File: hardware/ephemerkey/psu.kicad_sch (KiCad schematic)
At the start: 24 parts, among them J3 USB-C, J4 BAT 1S Li-ion, J5 USB-C (vert), Q1 AO3401A, U2 TPS63900DSKR, U3 USBLC6-2SC6, U4 MCP73831-2-OT

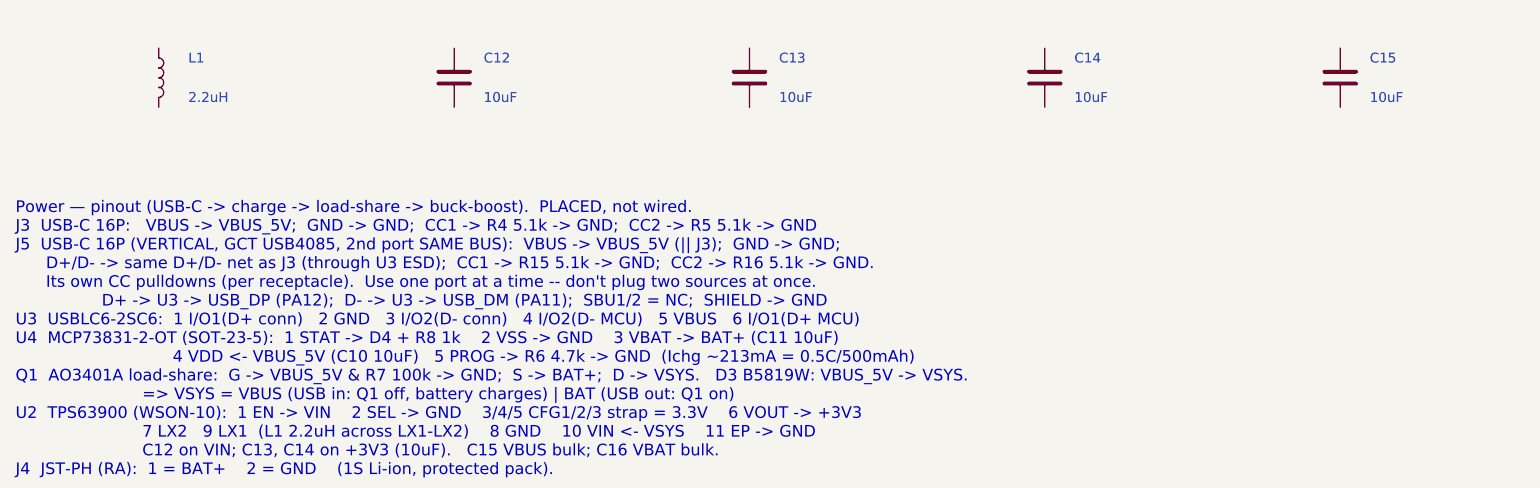
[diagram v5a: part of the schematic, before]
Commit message: ephemerkey: 2nd USB-C -> vertical GT-USB-7051A (C2843970), KiCad footprint
USB4085 was horizontal (GCT drawing: 'Dip Type, PCB Top Mount' -- cable inserts
parallel to the board), not the upright connector needed. Swap J5 to the
G-Switch GT-USB-7051A (C2843970): true vertical/upright SMT USB-C that sticks up
off the board, 16-pin USB2.0, ~3.5k JLCPCB stock, with a bundled KiCad footprint
(USB_C_Receptacle_G-Switch_GT-USB-7051x) + 3D model. Same symbol/bus as J3.

Co-Authored-By: Claude Opus 4.8 (1M context) <noreply@anthropic.com>
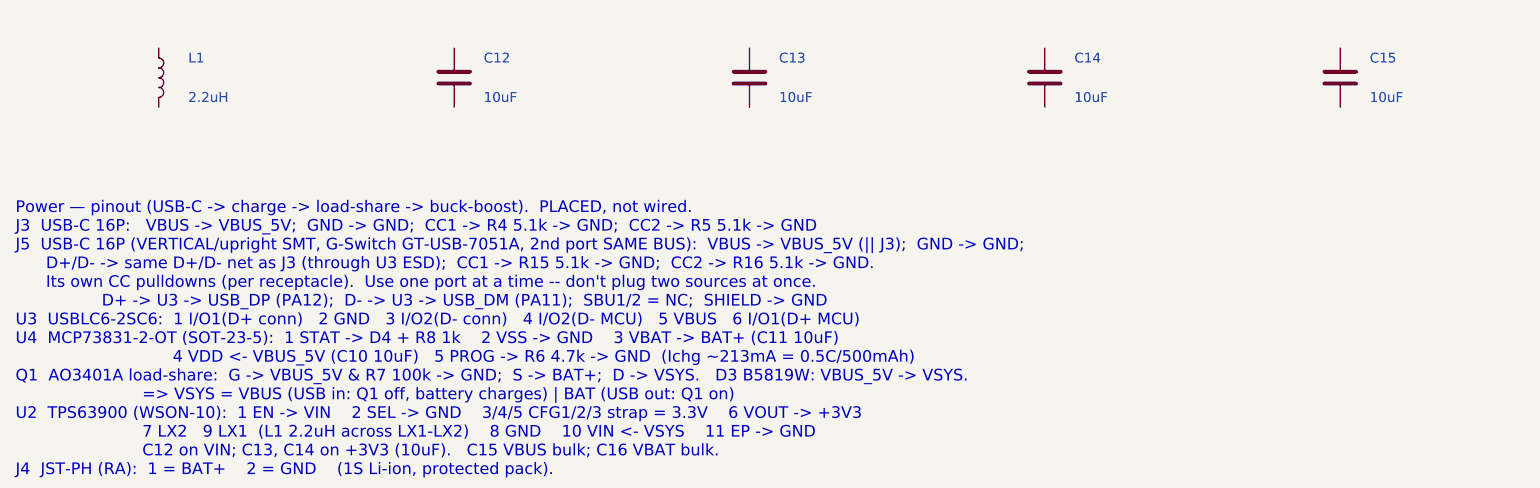
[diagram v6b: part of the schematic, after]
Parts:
- J5: footprint Connector_USB:USB_C_Receptacle_GCT_USB4085 -> Connector_USB:USB_C_Receptacle_G-Switch_GT-USB-7051x; LCSC C7095263 -> C2843970; MPN USB4085-GF-A -> GT-USB-7051A; Manufacturer GCT -> G-Switch
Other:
- note added: "Power — pinout (USB-C -> charge -> load-share -> buck-boost). PLACED, not wired. J3 USB-C 16P: VBUS -> VBUS_5V; GND -> GND; CC1 -> R4 5.1k -> GND; CC2 -> R5 5.1k -> GND J5 USB-C 16P (VERTICAL/upright SMT, G-Switch GT-USB-7051A, 2nd port SAME BUS): VBUS -> VBUS_5V (|| J3); GND -> GND; D+/D- -> same D+/D- net as J3 (through U3 ESD); CC1 -> R15 5.1k -> GND; CC2 -> R16 5.1k -> GND. Its own CC pulldow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"
- note removed: "Power — pinout (USB-C -> charge -> load-share -> buck-boost). PLACED, not wired. J3 USB-C 16P: VBUS -> VBUS_5V; GND -> GND; CC1 -> R4 5.1k -> GND; CC2 -> R5 5.1k -> GND J5 USB-C 16P (VERTICAL, GCT USB4085, 2nd port SAME BUS): VBUS -> VBUS_5V (|| J3); GND -> GND; D+/D- -> same D+/D- net as J3 (through U3 ESD); CC1 -> R15 5.1k -> GND; CC2 -> R16 5.1k -> GND. Its own CC pulldowns (per receptacle). U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"

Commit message: ephemerkey: vendor 3D model for the vertical USB-C (GT-USB-7051A)
The KiCad footprint for GT-USB-7051x references a STEP that's absent from this
(partial) 3D-model install. Fetched the model for C2843970 via easyeda2kicad
(EasyEDA/LCSC) -> lib/3dmodels/USB_C_GT-USB-7051A.step (2.3MB STEP), and added a
project footprint copy ephemerkey:USB_C_Receptacle_G-Switch_GT-USB-7051x with its
(model ...) repointed at the vendored file. J5 now uses the project footprint.
Verify model offset/rotation in the 3D viewer at layout (EasyEDA origin).

Co-Authored-By: Claude Opus 4.8 (1M context) <noreply@anthropic.com>
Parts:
- J5: footprint Connector_USB:USB_C_Receptacle_G-Switch_GT-USB-7051x -> ephemerkey:USB_C_Receptacle_G-Switch_GT-USB-7051x
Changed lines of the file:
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@@
 		(instances
 			(project "ephemerkey"
-				(path "/e1000000-0000-4000-8000-000000000001/9c958eea-92af-4fab-91f9-b500de8c2eb3"
+				(path "/e1000000-0000-4000-8000-000000000001/1a9d986c-45f1-4170-b653-57058bfaa0ea"
 					(reference "J3")
 					(unit 1)
@@
 		(instances
 			(project "ephemerkey"
-				(path "/e1000000-0000-4000-8000-000000000001/9c958eea-92af-4fab-91f9-b500de8c2eb3"
+				(path "/e1000000-0000-4000-8000-000000000001/1a9d986c-45f1-4170-b653-57058bfaa0ea"
 					(reference "J4")
 					(unit 1)
@@
 		(instances
 			(project "ephemerkey"
-				(path "/e1000000-0000-4000-8000-000000000001/9c958eea-92af-4fab-91f9-b500de8c2eb3"
+				(path "/e1000000-0000-4000-8000-000000000001/1a9d986c-45f1-4170-b653-57058bfaa0ea"
 					(reference "U2")
 					(unit 1)
@@
 			(effects (font (size 1.27 1.27)) (justify left))
 		)
-		(property "Footprint" "Connector_USB:USB_C_Receptacle_G-Switch_GT-USB-7051x"
+		(property "Footprint" "ephemerkey:USB_C_Receptacle_G-Switch_GT-USB-7051x"
 			(at 335.2800 55.8800 0)
 			(effects (font (size 1.27 1.27))) (hide yes)
@@
 		(instances
 			(project "ephemerkey"
-				(path "/e1000000-0000-4000-8000-000000000001/9c958eea-92af-4fab-91f9-b500de8c2eb3"
+				(path "/e1000000-0000-4000-8000-000000000001/1a9d986c-45f1-4170-b653-57058bfaa0ea"
 					(reference "J5")
 					(unit 1)
@@
 		(instances
 			(project "ephemerkey"
-				(path "/e1000000-0000-4000-8000-000000000001/9c958eea-92af-4fab-91f9-b500de8c2eb3"
+				(path "/e1000000-0000-4000-8000-000000000001/1a9d986c-45f1-4170-b653-57058bfaa0ea"
 					(reference "U3")
 					(unit 1)
@@
 		(instances
 			(project "ephemerkey"
-				(path "/e1000000-0000-4000-8000-000000000001/9c958eea-92af-4fab-91f9-b500de8c2eb3"
+				(path "/e1000000-0000-4000-8000-000000000001/1a9d986c-45f1-4170-b653-57058bfaa0ea"
 					(reference "R4")
 					(unit 1)
@@
 		(instances
 			(project "ephemerkey"
-				(path "/e1000000-0000-4000-8000-000000000001/9c958eea-92af-4fab-91f9-b500de8c2eb3"
+				(path "/e1000000-0000-4000-8000-000000000001/1a9d986c-45f1-4170-b653-57058bfaa0ea"
 					(reference "R5")
 					(unit 1)
@@
 		(instances
 			(project "ephemerkey"
-				(path "/e1000000-0000-4000-8000-000000000001/9c958eea-92af-4fab-91f9-b500de8c2eb3"
+				(path "/e1000000-0000-4000-8000-000000000001/1a9d986c-45f1-4170-b653-57058bfaa0ea"
 					(reference "U4")
 					(unit 1)
@@
 		(instances
 			(project "ephemerkey"
-				(path "/e1000000-0000-4000-8000-000000000001/9c958eea-92af-4fab-91f9-b500de8c2eb3"
+				(path "/e1000000-0000-4000-8000-000000000001/1a9d986c-45f1-4170-b653-57058bfaa0ea"
 					(reference "R6")
 					(unit 1)
@@
 		(instances
 			(project "ephemerkey"
-				(path "/e1000000-0000-4000-8000-000000000001/9c958eea-92af-4fab-91f9-b500de8c2eb3"
+				(path "/e1000000-0000-4000-8000-000000000001/1a9d986c-45f1-4170-b653-57058bfaa0ea"
 					(reference "C10")
 					(unit 1)
@@
 		(instances
 			(project "ephemerkey"
-				(path "/e1000000-0000-4000-8000-000000000001/9c958eea-92af-4fab-91f9-b500de8c2eb3"
+				(path "/e1000000-0000-4000-8000-000000000001/1a9d986c-45f1-4170-b653-57058bfaa0ea"
 					(reference "C11")
 					(unit 1)
@@
 		(instances
 			(project "ephemerkey"
-				(path "/e1000000-0000-4000-8000-000000000001/9c958eea-92af-4fab-91f9-b500de8c2eb3"
+				(path "/e1000000-0000-4000-8000-000000000001/1a9d986c-45f1-4170-b653-57058bfaa0ea"
 					(reference "Q1")
 					(unit 1)
@@
 		(instances
 			(project "ephemerkey"
-				(path "/e1000000-0000-4000-8000-000000000001/9c958eea-92af-4fab-91f9-b500de8c2eb3"
+				(path "/e1000000-0000-4000-8000-000000000001/1a9d986c-45f1-4170-b653-57058bfaa0ea"
 					(reference "D3")
 					(unit 1)
@@
 		(instances
 			(project "ephemerkey"
-				(path "/e1000000-0000-4000-8000-000000000001/9c958eea-92af-4fab-91f9-b500de8c2eb3"
+				(path "/e1000000-0000-4000-8000-000000000001/1a9d986c-45f1-4170-b653-57058bfaa0ea"
 					(reference "R7")
 					(unit 1)
@@
 		(instances
 			(project "ephemerkey"
-				(path "/e1000000-0000-4000-8000-000000000001/9c958eea-92af-4fab-91f9-b500de8c2eb3"
+				(path "/e1000000-0000-4000-8000-000000000001/1a9d986c-45f1-4170-b653-57058bfaa0ea"
 					(reference "L1")
 					(unit 1)
@@
 		(instances
 			(project "ephemerkey"
-				(path "/e1000000-0000-4000-8000-000000000001/9c958eea-92af-4fab-91f9-b500de8c2eb3"
+				(path "/e1000000-0000-4000-8000-000000000001/1a9d986c-45f1-4170-b653-57058bfaa0ea"
 					(reference "C12")
 					(unit 1)
@@
 		(instances
 			(project "ephemerkey"
-				(path "/e1000000-0000-4000-8000-000000000001/9c958eea-92af-4fab-91f9-b500de8c2eb3"
+				(path "/e1000000-0000-4000-8000-000000000001/1a9d986c-45f1-4170-b653-57058bfaa0ea"
 					(reference "C13")
 					(unit 1)
@@
 		(instances
 			(project "ephemerkey"
-				(path "/e1000000-0000-4000-8000-000000000001/9c958eea-92af-4fab-91f9-b500de8c2eb3"
+				(path "/e1000000-0000-4000-8000-000000000001/1a9d986c-45f1-4170-b653-57058bfaa0ea"
 					(reference "C14")
 					(unit 1)
@@
 		(instances
 			(project "ephemerkey"
-				(path "/e1000000-0000-4000-8000-000000000001/9c958eea-92af-4fab-91f9-b500de8c2eb3"
+				(path "/e1000000-0000-4000-8000-000000000001/1a9d986c-45f1-4170-b653-57058bfaa0ea"
 					(reference "C15")
 					(unit 1)
@@
 		(instances
 			(project "ephemerkey"
-				(path "/e1000000-0000-4000-8000-000000000001/9c958eea-92af-4fab-91f9-b500de8c2eb3"
+				(path "/e1000000-0000-4000-8000-000000000001/1a9d986c-45f1-4170-b653-57058bfaa0ea"
 					(reference "C16")
 					(unit 1)
@@
 		(instances
 			(project "ephemerkey"
-				(path "/e1000000-0000-4000-8000-000000000001/9c958eea-92af-4fab-91f9-b500de8c2eb3"
+				(path "/e1000000-0000-4000-8000-000000000001/1a9d986c-45f1-4170-b653-57058bfaa0ea"
 					(reference "D4")
 					(unit 1)
@@
 		(instances
 			(project "ephemerkey"
-				(path "/e1000000-0000-4000-8000-000000000001/9c958eea-92af-4fab-91f9-b500de8c2eb3"
+				(path "/e1000000-0000-4000-8000-000000000001/1a9d986c-45f1-4170-b653-57058bfaa0ea"
 					(reference "R8")
 					(unit 1)
@@
 		(instances
 			(project "ephemerkey"
-				(path "/e1000000-0000-4000-8000-000000000001/9c958eea-92af-4fab-91f9-b500de8c2eb3"
+				(path "/e1000000-0000-4000-8000-000000000001/1a9d986c-45f1-4170-b653-57058bfaa0ea"
 					(reference "R15")
 					(unit 1)
@@
 		(instances
 			(project "ephemerkey"
-				(path "/e1000000-0000-4000-8000-000000000001/9c958eea-92af-4fab-91f9-b500de8c2eb3"
+				(path "/e1000000-0000-4000-8000-000000000001/1a9d986c-45f1-4170-b653-57058bfaa0ea"
 					(reference "R16")
 					(unit 1)

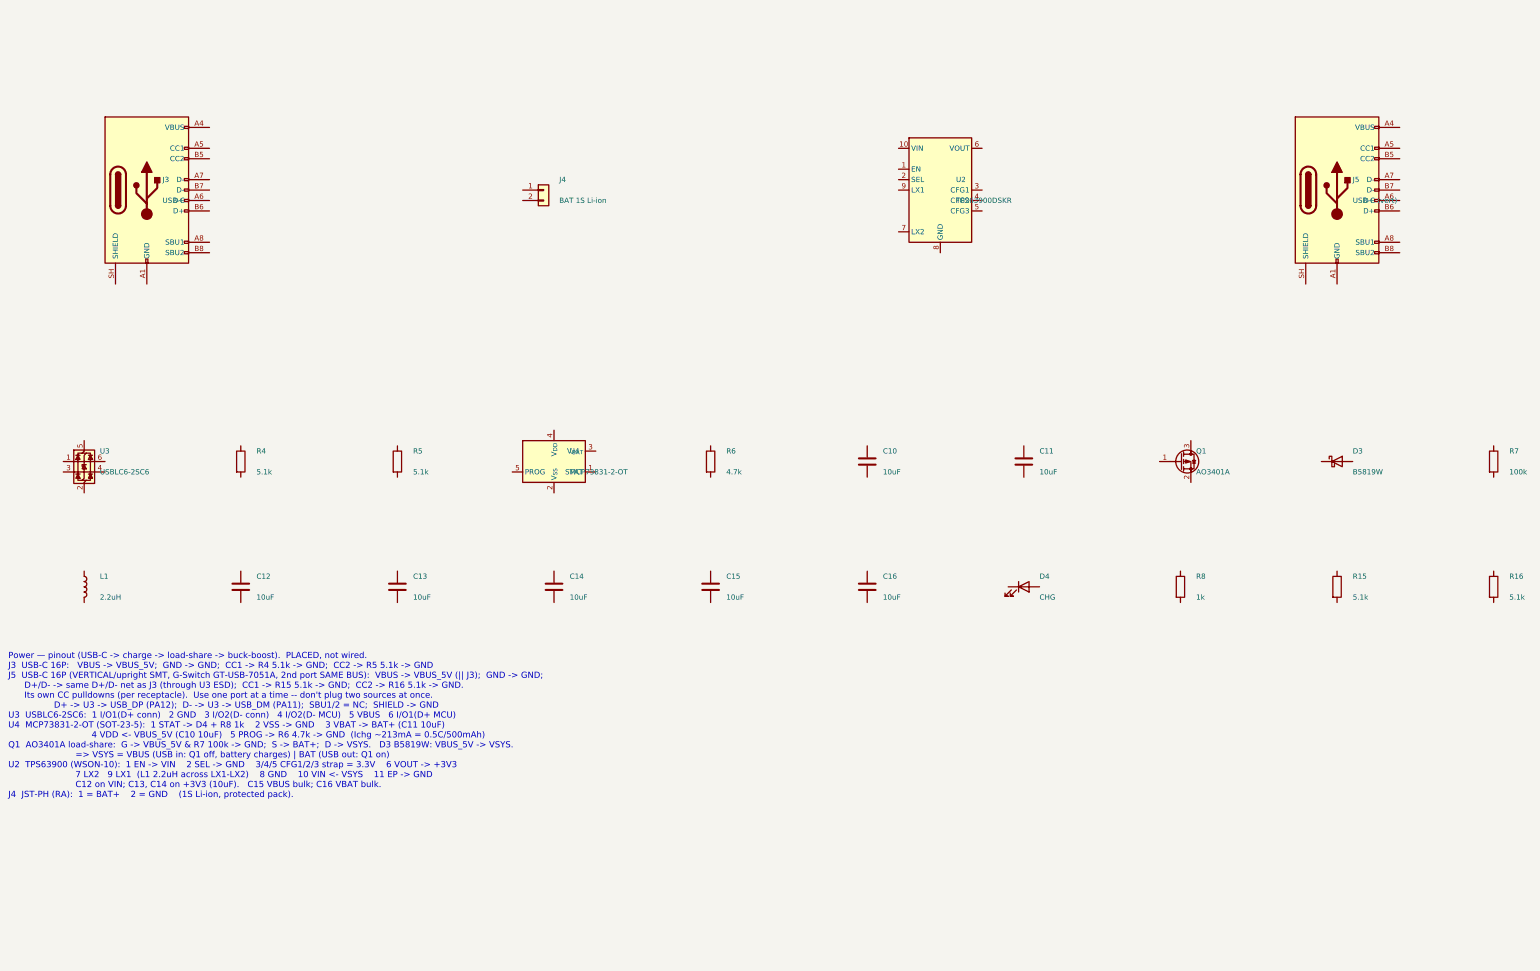
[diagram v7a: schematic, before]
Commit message: hardware: fix PSU load-share S/D, make all sheet notes monospace
The PSU wiring note specified Q1 (AO3401A load-share PMOS) as S=BAT+,
D=VSYS. A PMOS body diode conducts D->S, so that orientation points the
diode VSYS -> BAT+: with USB attached VSYS sits ~4.7V (VBUS - D3) against
a 3.0-4.2V cell, forward-biasing it and dumping uncontrolled current into
the battery, bypassing the MCP73831 charger entirely.

Correct assignment is D=BAT+, S=VSYS, so the body diode points BAT+ ->
VSYS: the battery always reaches the load, and USB can never back-feed
the cell. Q1 was placed but never wired (all three pins are unconnected
in the netlist), so this is a spec fix ahead of wiring, not a board
change. The lock's Q3 is a high-side switch and deliberately uses the
opposite S/D assignment; the note now says so, to stop the two being
"reconciled" by pattern-matching.

Also relaid the PSU note as a two-column table and gave every sheet note
the Courier New face the generator already emits (kschgen NOTE_FONT, added
in 43a6067). The sheets predate that commit, so their notes rendered in
KiCad's variable-width stroke font and the space-padded pin tables did not
line up. Font only on the other six notes -- text is untouched.

Verified: kicad-cli netlists for both boards are byte-identical before and
after (ephemerkey 259 nodes, lock 131 nodes) once the export timestamp is
excluded; no non-font lines changed in any sheet; all sheets re-rendered
and the notes fit inside the page frame.

The four ephemerkey sheets also carry pre-existing eeschema reformatting
(expanded lib_symbols) that was already in the working tree.

Co-Authored-By: Claude Opus 4.8 (1M context) <noreply@anthropic.com>
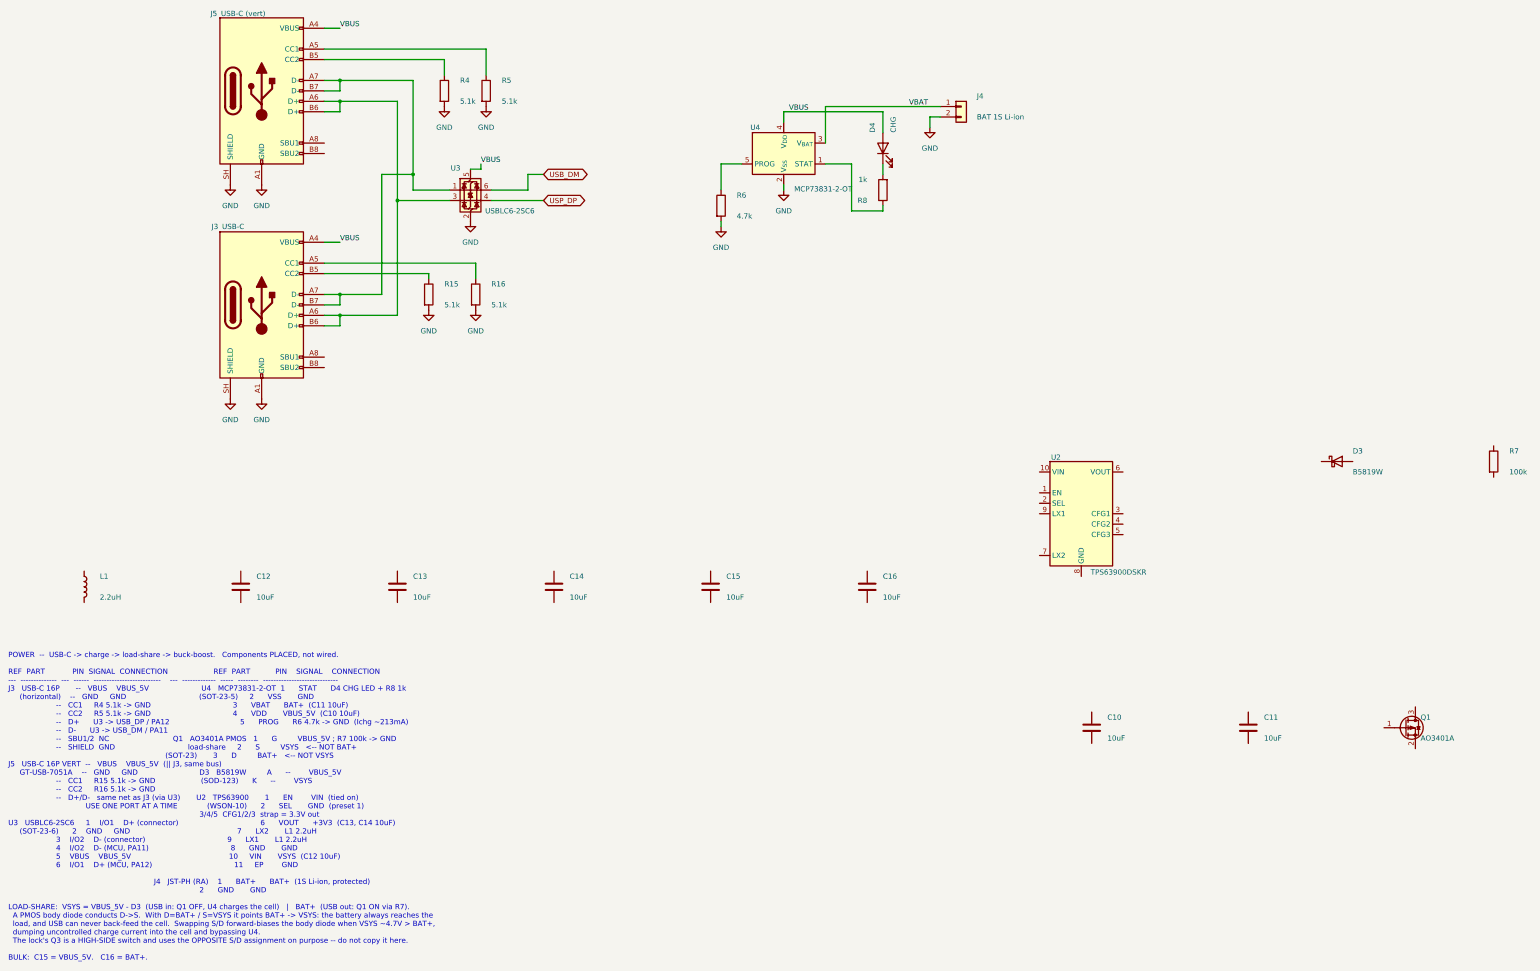
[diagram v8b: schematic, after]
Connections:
- net at R16.1: now also J3.A5 (CC1)
- net GND: now reaches R16.2
- net GND: now also J3.A1 (GND), J3.A12 (GND), J3.B1 (GND), J3.B12 (GND), J3.SH (SHIELD), J4.2 (Pin_2), J5.A1 (GND), J5.A12 (GND), J5.B1 (GND), J5.B12 (GND), J5.SH (SHIELD), R15.2, R4.2, R5.2, R6.2, U3.2 (GND), U4.2 (V_{SS})
- net VBAT: now reaches J4.1 (Pin_1)
- net VBAT: now also U4.3 (V_{BAT})
- net at R15.1: now also J3.B5 (CC2)
- net at R8.1: now also U4.1 (STAT)
- net at R8.2: now also D4.1 (K)
- net VBUS: now reaches J5.A4 (VBUS), J5.A9 (VBUS), J5.B4 (VBUS), J5.B9 (VBUS)
- net VBUS: now also D4.2 (A), J3.A4 (VBUS), J3.A9 (VBUS), J3.B4 (VBUS), J3.B9 (VBUS), U3.5 (VBUS), U4.4 (V_{DD})
- net at J5.A5 (CC1): now also R5.1
- net at J5.A6 (D+): now also J3.A6 (D+), J3.B6 (D+), J5.B6 (D+), U3.3 (I/O2)
- net at J5.A7 (D-): now also J3.A7 (D-), J3.B7 (D-), J5.B7 (D-), U3.1 (I/O1)
- net at J5.B5 (CC2): now also R4.1
- net at U4.5 (PROG): now also R6.1
- net USP_DP: now reaches U3.4 (I/O2)
- net USB_DM: now reaches U3.6 (I/O1)
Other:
- note added: "POWER -- USB-C -> charge -> load-share -> buck-boost. Components PLACED, not wired. REF PART PIN SIGNAL CONNECTION REF PART PIN SIGNAL CONNECTION --- -------------- --- ------ -------------------------- --- ------------- ----- -------- ----------------------------- J3 USB-C 16P -- VBUS VBUS_5V U4 MCP73831-2-OT 1 STAT D4 CHG LED + R8 1k (horizontal) -- GND GND (SOT-23-5) 2 VSS GND -- CC1 R4 5.1k -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"
- note removed: "Power — pinout (USB-C -> charge -> load-share -> buck-boost). PLACED, not wired. J3 USB-C 16P: VBUS -> VBUS_5V; GND -> GND; CC1 -> R4 5.1k -> GND; CC2 -> R5 5.1k -> GND J5 USB-C 16P (VERTICAL/upright SMT, G-Switch GT-USB-7051A, 2nd port SAME BUS): VBUS -> VBUS_5V (|| J3); GND -> GND; D+/D- -> same D+/D- net as J3 (through U3 ESD); CC1 -> R15 5.1k -> GND; CC2 -> R16 5.1k -> GND. Its own CC pulldow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"
- moved on the sheet: C10, C11, D4, J3, J4, J5, Q1, R15, R16, R4, R5, R6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
